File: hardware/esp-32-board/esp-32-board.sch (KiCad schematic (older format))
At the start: 12 parts, among them J1 Conn_Arduino_UNO_R3, J2 Conn_02x03_Odd_Even, J3 ESP-PROG-Program, J4 ESP-PROG-Debug, SW1 SW_Push, SW2 SW_Push, U1 ESP32-WROOM-32

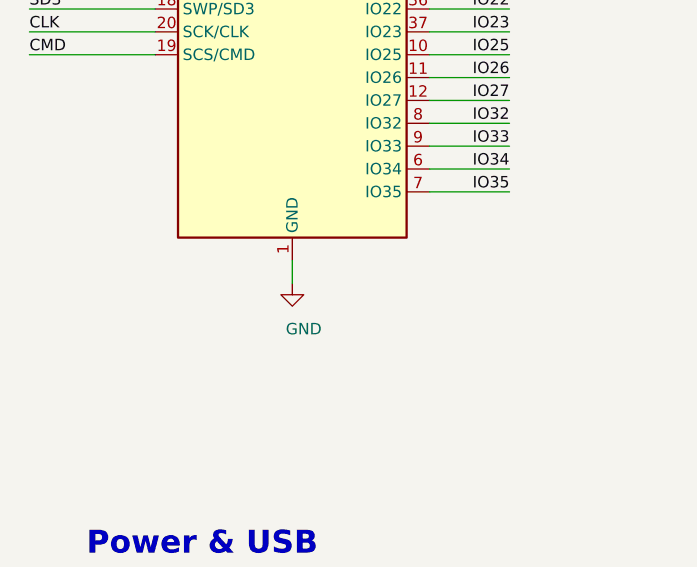
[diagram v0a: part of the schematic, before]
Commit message: Improve heat dissipation
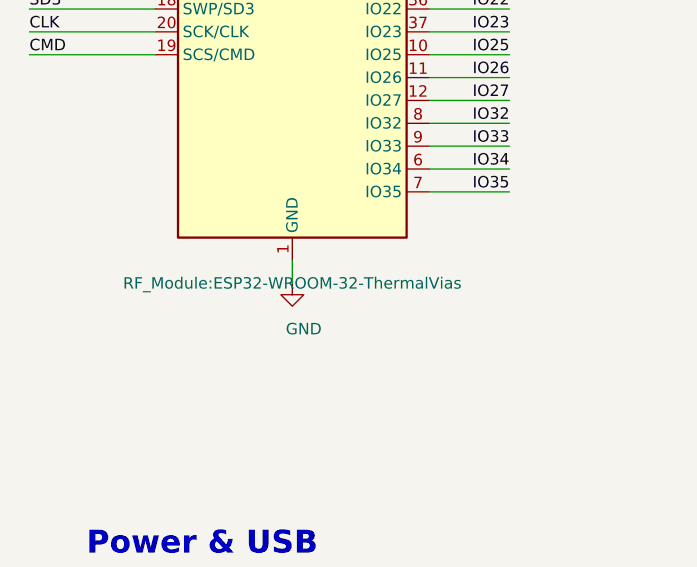
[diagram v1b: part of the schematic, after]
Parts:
- U1: footprint RF_Module:ESP32-WROOM-32 -> RF_Module:ESP32-WROOM-32-ThermalVias
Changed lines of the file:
@@
 F 0 "U1" H 1600 4400 50  0000 C CNN
 F 1 "ESP32-WROOM-32" H 2700 4400 50  0000 C CNN
-F 2 "RF_Module:ESP32-WROOM-32" H 2100 1500 50  0001 C CNN
+F 2 "RF_Module:ESP32-WROOM-32-ThermalVias" H 2100 1500 50  0000 C CNN
 F 3 "https://www.espressif.com/sites/default/files/documentation/esp32-wroom-32_datasheet_en.pdf" H 1800 3050 50  0001 C CNN
 	1    2100 3000

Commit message: Use THT connector for pins 17-21
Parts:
- J2: footprint Connector_PinSocket_2.54mm:PinSocket_1x06_P2.54mm_Vertical_SMD_Pin1Left -> Connector_PinSocket_2.54mm:PinSocket_1x06_P2.54mm_Vertical
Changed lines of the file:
@@
 F 0 "J2" H 10000 2800 50  0000 C CNN
 F 1 "Conn_02x03_Odd_Even" H 10000 2000 50  0000 C CNN
-F 2 "Connector_PinSocket_2.54mm:PinSocket_1x06_P2.54mm_Vertical_SMD_Pin1Left" H 10000 2450 50  0001 C CNN
+F 2 "Connector_PinSocket_2.54mm:PinSocket_1x06_P2.54mm_Vertical" H 10000 2450 50  0001 C CNN
 F 3 "~" H 10000 2450 50  0001 C CNN
 F 4 "N/A" H 10000 2450 50  0001 C CNN "Vendor"

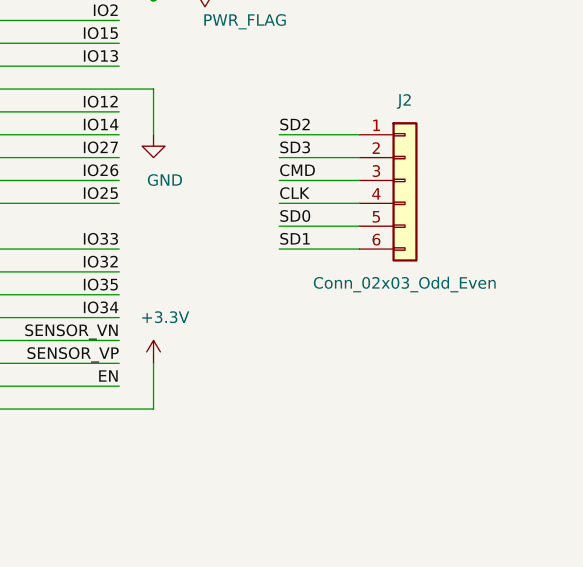
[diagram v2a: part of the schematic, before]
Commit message: Use FT232RL instead of CP2102N
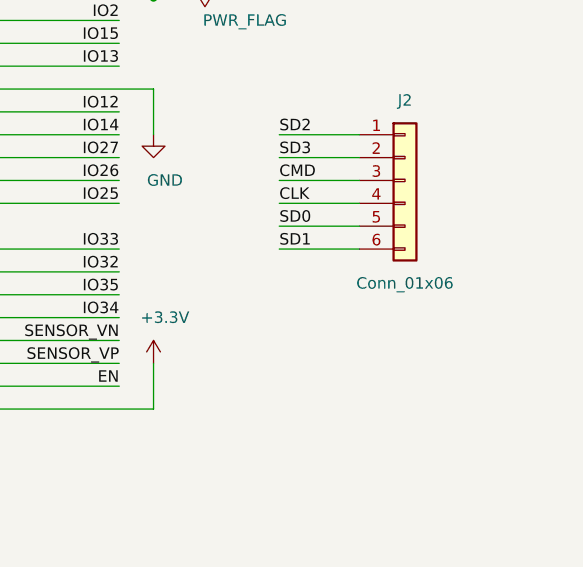
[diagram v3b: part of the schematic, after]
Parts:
- J2: value Conn_02x03_Odd_Even -> Conn_01x06
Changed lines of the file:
@@
 P 10000 2450
 F 0 "J2" H 10000 2800 50  0000 C CNN
-F 1 "Conn_02x03_Odd_Even" H 10000 2000 50  0000 C CNN
+F 1 "Conn_01x06" H 10000 2000 50  0000 C CNN
 F 2 "Connector_PinSocket_2.54mm:PinSocket_1x06_P2.54mm_Vertical" H 10000 2450 50  0001 C CNN
 F 3 "~" H 10000 2450 50  0001 C CNN

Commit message: Change connector to simpler (incompatible with Arduino, only similar)
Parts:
- J1: value Conn_Arduino_UNO_R3 -> MainConnector; footprint Module:Arduino_UNO_R3_WithMountingHoles -> project_components:MainConnector; symbol Connector:Conn_Arduino_UNO_R3 -> project_components:MainConnector
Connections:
- wire segments 140 -> 142
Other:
- moved on the sheet: J1
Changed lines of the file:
@@
 Text Label 8750 2750 2    50   ~ 0
 IO33
+Text Label 8750 2650 2    50   ~ 0
+IO25
 Text Label 8750 2550 2    50   ~ 0
-IO25
+IO26
 Text Label 8750 2450 2    50   ~ 0
-IO26
+IO27
 Text Label 8750 2350 2    50   ~ 0
-IO27
+IO14
 Text Label 8750 2250 2    50   ~ 0
-IO14
-Text Label 8750 2150 2    50   ~ 0
 IO12
 Wire Wire Line
@@
 	8200 2750 8750 2750
 Wire Wire Line
-	8750 2550 8200 2550
-Wire Wire Line
-	8200 2450 8750 2450
-Wire Wire Line
-	8200 2250 8750 2250
-Wire Wire Line
-	8750 2150 8200 2150
-Text Label 8750 1950 2    50   ~ 0
+	8750 2650 8200 2650
+Wire Wire Line
+	8200 2550 8750 2550
+Wire Wire Line
+	8200 2350 8750 2350
+Wire Wire Line
+	8750 2250 8200 2250
+Text Label 8750 2150 2    50   ~ 0
 IO13
 Text Label 9450 2250 0    50   ~ 0
@@
 L power:GND #PWR016
 U 1 1 5FBE8B3A
-P 8900 2250
-F 0 "#PWR016" H 8900 2000 50  0001 C CNN
-F 1 "GND" H 8950 2050 50  0000 C CNN
-F 2 "" H 8900 2250 50  0001 C CNN
-F 3 "" H 8900 2250 50  0001 C CNN
-	1    8900 2250
+P 8900 2050
+F 0 "#PWR016" H 8900 1800 50  0001 C CNN
+F 1 "GND" H 8950 1850 50  0000 C CNN
+F 2 "" H 8900 2050 50  0001 C CNN
+F 3 "" H 8900 2050 50  0001 C CNN
+	1    8900 2050
 	1    0    0    -1
 $EndComp
@@
 Text Label 6850 2950 0    50   ~ 0
 IO21
+Text Label 6850 2850 0    50   ~ 0
+IO19
 Text Label 6850 2750 0    50   ~ 0
-IO19
+IO18
 Text Label 6850 2650 0    50   ~ 0
-IO18
+IO5
 Text Label 6850 2550 0    50   ~ 0
-IO5
+IO17
 Text Label 6850 2450 0    50   ~ 0
-IO17
+IO16
 Text Label 6850 2350 0    50   ~ 0
-IO16
+IO4
 Text Label 6850 2250 0    50   ~ 0
-IO4
-Text Label 6850 2150 0    50   ~ 0
 IO0
-Text Label 8750 1750 2    50   ~ 0
+Text Label 8750 1950 2    50   ~ 0
 IO2
-Text Label 8750 1850 2    50   ~ 0
+Text Label 8750 2050 2    50   ~ 0
 IO15
 Text Label 9450 2750 0    50   ~ 0
@@
 	7400 3050 6850 3050
 Wire Wire Line
+	7400 2850 6850 2850
+Wire Wire Line
 	7400 2750 6850 2750
 Wire Wire Line
 	7400 2650 6850 2650
 Wire Wire Line
-	7400 2550 6850 2550
-Wire Wire Line
-	7400 2350 6850 2350
-Wire Wire Line
-	6850 2250 7400 2250
-Wire Wire Line
-	7400 2150 6850 2150
-Wire Wire Line
-	8200 1850 8750 1850
+	7400 2450 6850 2450
+Wire Wire Line
+	6850 2350 7400 2350
+Wire Wire Line
+	7400 2250 6850 2250
+Wire Wire Line
+	8200 2050 8750 2050
 Wire Wire Line
 	9450 2750 9800 2750
@@
 	1500 3500 950  3500
 Wire Wire Line
-	8750 1950 8200 1950
+	8750 2150 8200 2150
 Wire Wire Line
 	9800 2250 9450 2250
@@
 $EndComp
 Wire Wire Line
-	8750 2350 8200 2350
+	8750 2450 8200 2450
 Wire Wire Line
 	8750 2850 8200 2850
@@
 	7400 2950 6850 2950
 Wire Wire Line
-	7400 2450 6850 2450
+	7400 2550 6850 2550
 $Comp
 L Connector:ESP-PROG-Program J3
@@
 	9500 5500 9800 5500
 $Comp
-L Connector:Conn_Arduino_UNO_R3 J1
+L project_components:MainConnector J1
 U 1 1 600797C7
 P 7800 2550
 F 0 "J1" H 7800 3700 50  0000 C CNN
-F 1 "Conn_Arduino_UNO_R3" H 7800 3600 50  0000 C CNN
-F 2 "Module:Arduino_UNO_R3_WithMountingHoles" H 7600 2050 50  0001 C CNN
+F 1 "MainConnector" H 7800 3600 50  0000 C CNN
+F 2 "project_components:MainConnector" H 7600 2050 50  0001 C CNN
 F 3 "~" H 7600 2050 50  0001 C CNN
 F 4 "N/A" H 7800 2550 50  0001 C CNN "Vendor"
@@
 	8900 3450 8900 3250
 Wire Wire Line
-	8200 2050 8900 2050
-Wire Wire Line
-	8900 2050 8900 2250
-Wire Wire Line
-	8750 1750 8200 1750
+	8200 1850 8900 1850
+Wire Wire Line
+	8900 1850 8900 2050
+Wire Wire Line
+	8750 1950 8200 1950
 $Comp
 L power:+3.3V #PWR011
@@
 Wire Wire Line
 	900  6600 1250 6600
-Text Label 8750 1650 2    50   ~ 0
+Text Label 8750 1750 2    50   ~ 0
 VIN
 Wire Wire Line
@@
 L power:VDC #PWR015
 U 1 1 5FD163B8
-P 8900 1500
-F 0 "#PWR015" H 8900 1400 50  0001 C CNN
-F 1 "VDC" H 8950 1700 50  0000 C CNN
-F 2 "" H 8900 1500 50  0001 C CNN
-F 3 "" H 8900 1500 50  0001 C CNN
-	1    8900 1500
-	1    0    0    -1
-$EndComp
-Wire Wire Line
-	8900 1500 8900 1650
-Wire Wire Line
-	8200 1650 8900 1650
+P 8900 1600
+F 0 "#PWR015" H 8900 1500 50  0001 C CNN
+F 1 "VDC" H 8950 1800 50  0000 C CNN
+F 2 "" H 8900 1600 50  0001 C CNN
+F 3 "" H 8900 1600 50  0001 C CNN
+	1    8900 1600
+	1    0    0    -1
+$EndComp
+Wire Wire Line
+	8900 1600 8900 1750
+Wire Wire Line
+	8200 1750 8900 1750
 Wire Wire Line
 	4400 6700 5000 6700
@@
 L power:PWR_FLAG #FLG0102
 U 1 1 5FD02A12
-P 9050 1650
-F 0 "#FLG0102" H 9050 1725 50  0001 C CNN
-F 1 "PWR_FLAG" V 9150 1900 50  0000 C CNN
-F 2 "" H 9050 1650 50  0001 C CNN
-F 3 "~" H 9050 1650 50  0001 C CNN
-	1    9050 1650
+P 9050 1750
+F 0 "#FLG0102" H 9050 1825 50  0001 C CNN
+F 1 "PWR_FLAG" V 9150 2000 50  0000 C CNN
+F 2 "" H 9050 1750 50  0001 C CNN
+F 3 "~" H 9050 1750 50  0001 C CNN
+	1    9050 1750
 	0    1    1    0
 $EndComp
 Wire Wire Line
-	8900 1650 9050 1650
+	8900 1750 9050 1750
 $Comp
 L power:PWR_FLAG #FLG0103
@@
 Wire Wire Line
 	6700 3450 7400 3450
-Connection ~ 8900 1650
+Connection ~ 8900 1750
 Wire Wire Line
 	6700 3450 6600 3450
 Connection ~ 6700 3450
+$Comp
+L power:GND #PWR0101
+U 1 1 5FF57139
+P 6700 2250
+F 0 "#PWR0101" H 6700 2000 50  0001 C CNN
+F 1 "GND" H 6750 2050 50  0000 C CNN
+F 2 "" H 6700 2250 50  0001 C CNN
+F 3 "" H 6700 2250 50  0001 C CNN
+	1    6700 2250
+	1    0    0    -1
+$EndComp
+Wire Wire Line
+	7400 2150 6700 2150
+Wire Wire Line
+	6700 2150 6700 2250
 $EndSCHEMATC

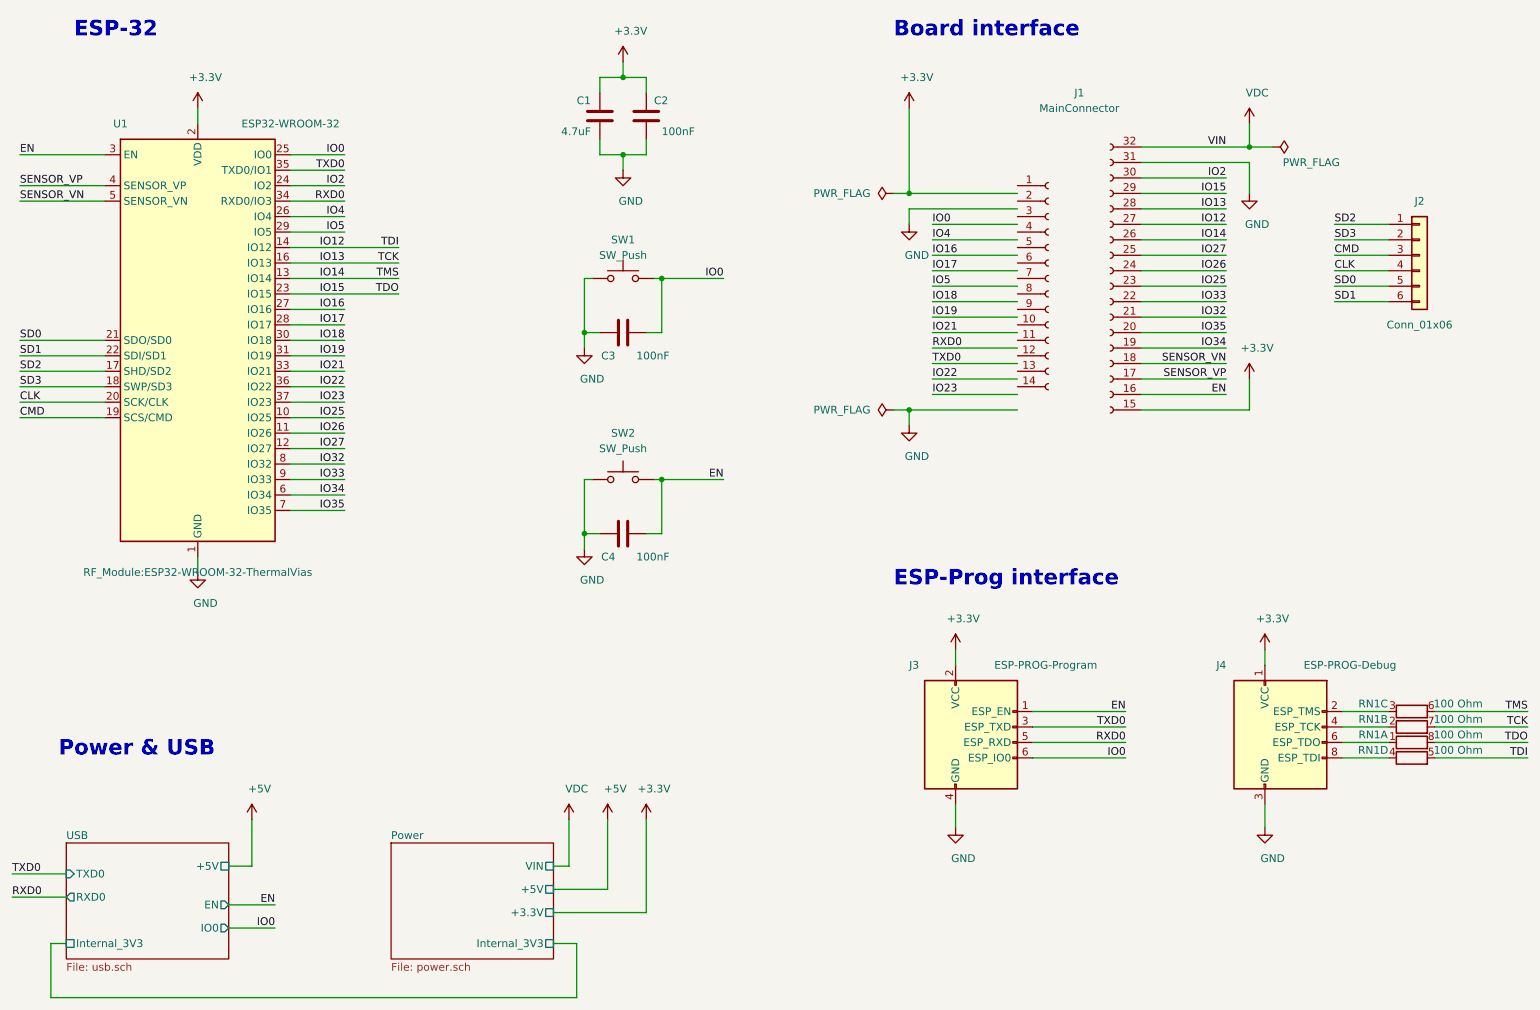
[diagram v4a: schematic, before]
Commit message: Fix ERC errors in schematic
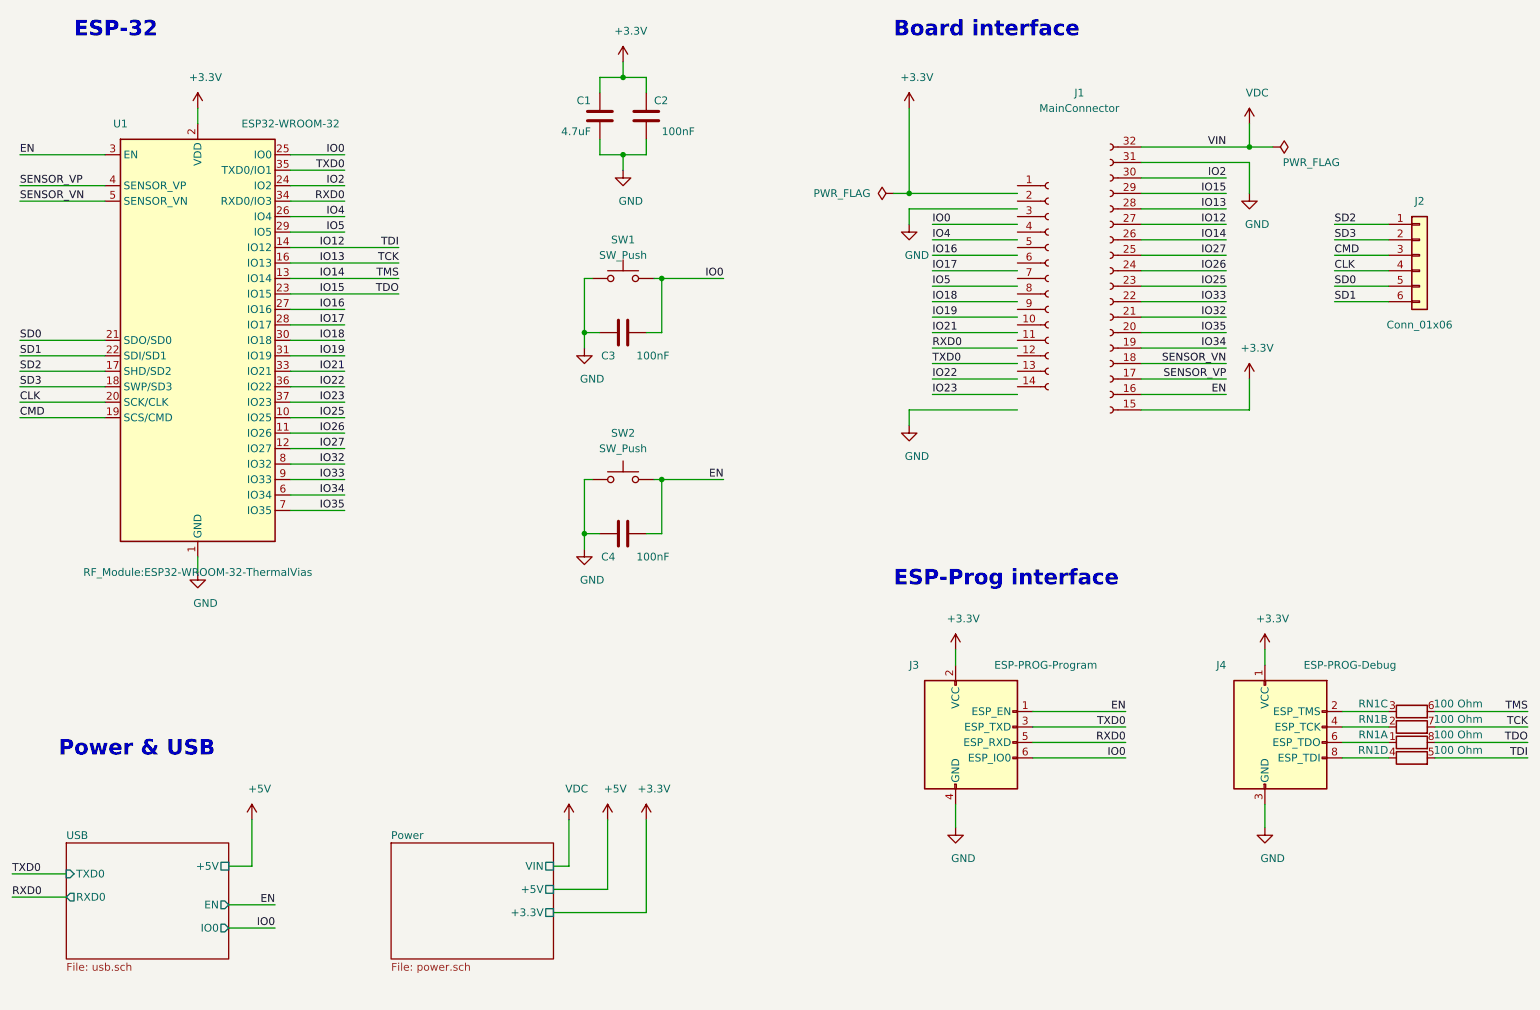
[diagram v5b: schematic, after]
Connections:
- wire segments 142 -> 136
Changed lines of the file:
@@
-	1    0    0    -1
-$EndComp
-$Comp
-L power:GND #PWR012
-U 1 1 5FC02DF9
-P 6700 3550
-F 0 "#PWR012" H 6700 3300 50  0001 C CNN
-F 1 "GND" H 6750 3350 50  0000 C CNN
-F 2 "" H 6700 3550 50  0001 C CNN
-F 3 "" H 6700 3550 50  0001 C CNN
-	1    6700 3550
 	1    0    0    -1
 $EndComp
@@
 $EndComp
 Wire Wire Line
-	6700 3450 6700 3550
-Wire Wire Line
 	8200 3450 8900 3450
 Wire Wire Line
@@
 F3 "+5V" U R 4400 6550 50
 F4 "+3.3V" U R 4400 6700 50
-F5 "Internal_3V3" U R 4400 6900 50
 $EndSheet
 $Sheet
@@
 F4 "TXD0" I L 1250 6450 50
 F5 "RXD0" O L 1250 6600 50
-F6 "Internal_3V3" U L 1250 6900 50
 F7 "+5V" U R 2300 6400 50
 $EndSheet
@@
 	1    0    0    -1
 $EndComp
-Wire Wire Line
-	4400 6900 4550 6900
-Wire Wire Line
-	4550 6900 4550 7250
-Wire Wire Line
-	4550 7250 1150 7250
-Wire Wire Line
-	1150 7250 1150 6900
-Wire Wire Line
-	1150 6900 1250 6900
 $Comp
 L power:+5V #PWR03
@@
 Text Notes 1300 1050 0    100  ~ 20
 ESP-32
-$Comp
-L power:PWR_FLAG #FLG0101
-U 1 1 5FCD3A56
-P 6600 3450
-F 0 "#FLG0101" H 6600 3525 50  0001 C CNN
-F 1 "PWR_FLAG" V 6600 3600 50  0000 L CNN
-F 2 "" H 6600 3450 50  0001 C CNN
-F 3 "~" H 6600 3450 50  0001 C CNN
-	1    6600 3450
-	0    -1   -1   0
-$EndComp
 Wire Wire Line
 	2100 1500 2100 1600
@@
 Wire Wire Line
 	2100 4400 2100 4500
-Wire Wire Line
-	6700 3450 7400 3450
 Connection ~ 8900 1750
-Wire Wire Line
-	6700 3450 6600 3450
-Connection ~ 6700 3450
 $Comp
 L power:GND #PWR0101
@@
 Wire Wire Line
 	6700 2150 6700 2250
+Wire Wire Line
+	6700 3450 7400 3450
+Wire Wire Line
+	6700 3450 6700 3550
+$Comp
+L power:GND #PWR012
+U 1 1 5FC02DF9
+P 6700 3550
+F 0 "#PWR012" H 6700 3300 50  0001 C CNN
+F 1 "GND" H 6750 3350 50  0000 C CNN
+F 2 "" H 6700 3550 50  0001 C CNN
+F 3 "" H 6700 3550 50  0001 C CNN
+	1    6700 3550
+	1    0    0    -1
+$EndComp
 $EndSCHEMATC

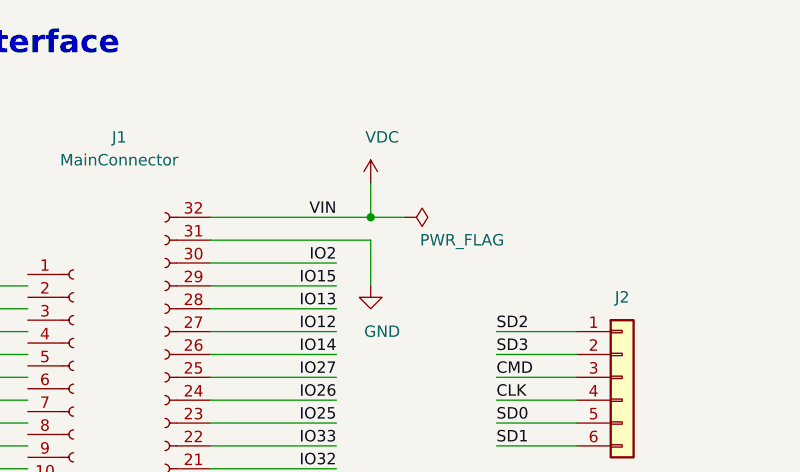
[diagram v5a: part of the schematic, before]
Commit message: Expose 5V instead of VIN on main connector
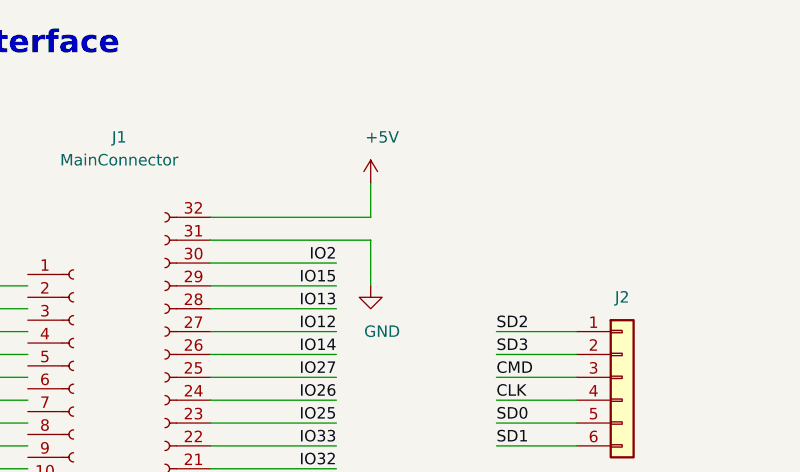
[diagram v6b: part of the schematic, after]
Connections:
- net labels removed: VIN
- wire segments 136 -> 135
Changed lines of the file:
@@
 Wire Wire Line
 	900  6600 1250 6600
-Text Label 8750 1750 2    50   ~ 0
-VIN
 Wire Wire Line
 	4400 6550 4750 6550
@@
 	1    0    0    -1
 $EndComp
-$Comp
-L power:VDC #PWR015
-U 1 1 5FD163B8
-P 8900 1600
-F 0 "#PWR015" H 8900 1500 50  0001 C CNN
-F 1 "VDC" H 8950 1800 50  0000 C CNN
-F 2 "" H 8900 1600 50  0001 C CNN
-F 3 "" H 8900 1600 50  0001 C CNN
-	1    8900 1600
-	1    0    0    -1
-$EndComp
-Wire Wire Line
-	8900 1600 8900 1750
-Wire Wire Line
-	8200 1750 8900 1750
 Wire Wire Line
 	4400 6700 5000 6700
@@
 	5000 6100 5000 6700
 $Comp
-L power:PWR_FLAG #FLG0102
-U 1 1 5FD02A12
-P 9050 1750
-F 0 "#FLG0102" H 9050 1825 50  0001 C CNN
-F 1 "PWR_FLAG" V 9150 2000 50  0000 C CNN
-F 2 "" H 9050 1750 50  0001 C CNN
-F 3 "~" H 9050 1750 50  0001 C CNN
-	1    9050 1750
-	0    1    1    0
-$EndComp
-Wire Wire Line
-	8900 1750 9050 1750
-$Comp
 L power:PWR_FLAG #FLG0103
 U 1 1 5FD0B643
@@
 Wire Wire Line
 	2100 4400 2100 4500
-Connection ~ 8900 1750
 $Comp
 L power:GND #PWR0101
@@
 	1    0    0    -1
 $EndComp
+$Comp
+L power:+5V #PWR0102
+U 1 1 5FFB2CC9
+P 8900 1600
+F 0 "#PWR0102" H 8900 1450 50  0001 C CNN
+F 1 "+5V" H 8950 1800 50  0000 C CNN
+F 2 "" H 8900 1600 50  0001 C CNN
+F 3 "" H 8900 1600 50  0001 C CNN
+	1    8900 1600
+	1    0    0    -1
+$EndComp
+Wire Wire Line
+	8200 1750 8900 1750
+Wire Wire Line
+	8900 1600 8900 1750
 $EndSCHEMATC
